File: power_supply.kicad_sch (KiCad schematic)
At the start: 24 parts, among them J1 Banana Plug, U1 MAX200008A

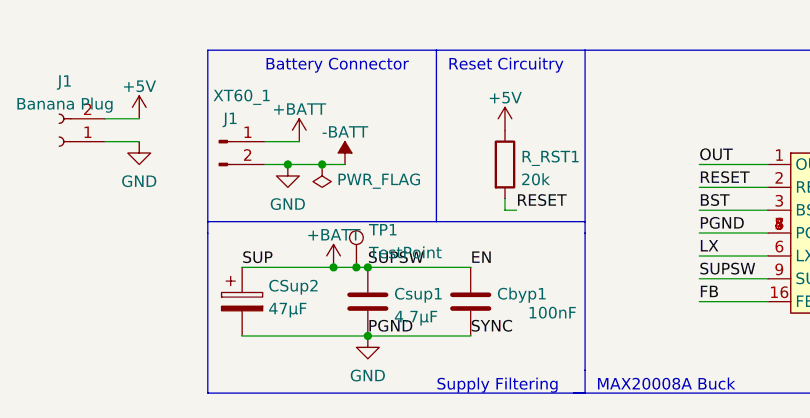
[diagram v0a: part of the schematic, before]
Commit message: MAX20008 dev board update
Added reverse polarity protection diode on the input.
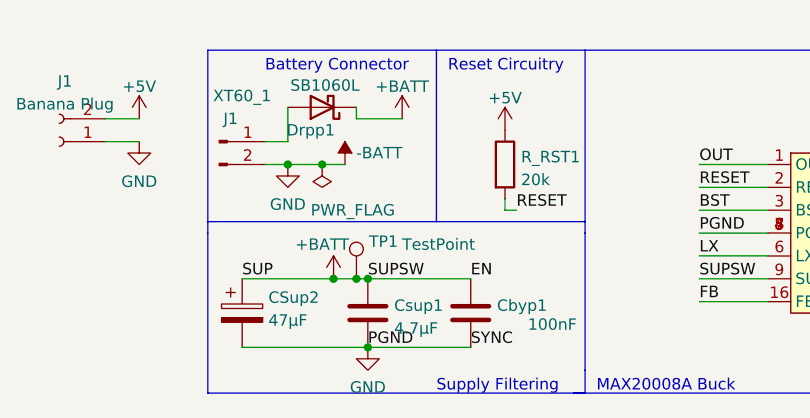
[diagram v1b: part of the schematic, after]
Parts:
- added Drpp1: SB1060L, footprints:TO_277B, symbol Device:D_Schottky
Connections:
- net +BATT: now also Drpp1.1 (K); no longer XT60_1.1 (Pin_1)
- new net: Drpp1.2 (A), XT60_1.1 (Pin_1)
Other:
- moved on the sheet: CSup2, Cbyp1, Csup1, TP1
